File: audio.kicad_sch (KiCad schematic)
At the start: 29 parts

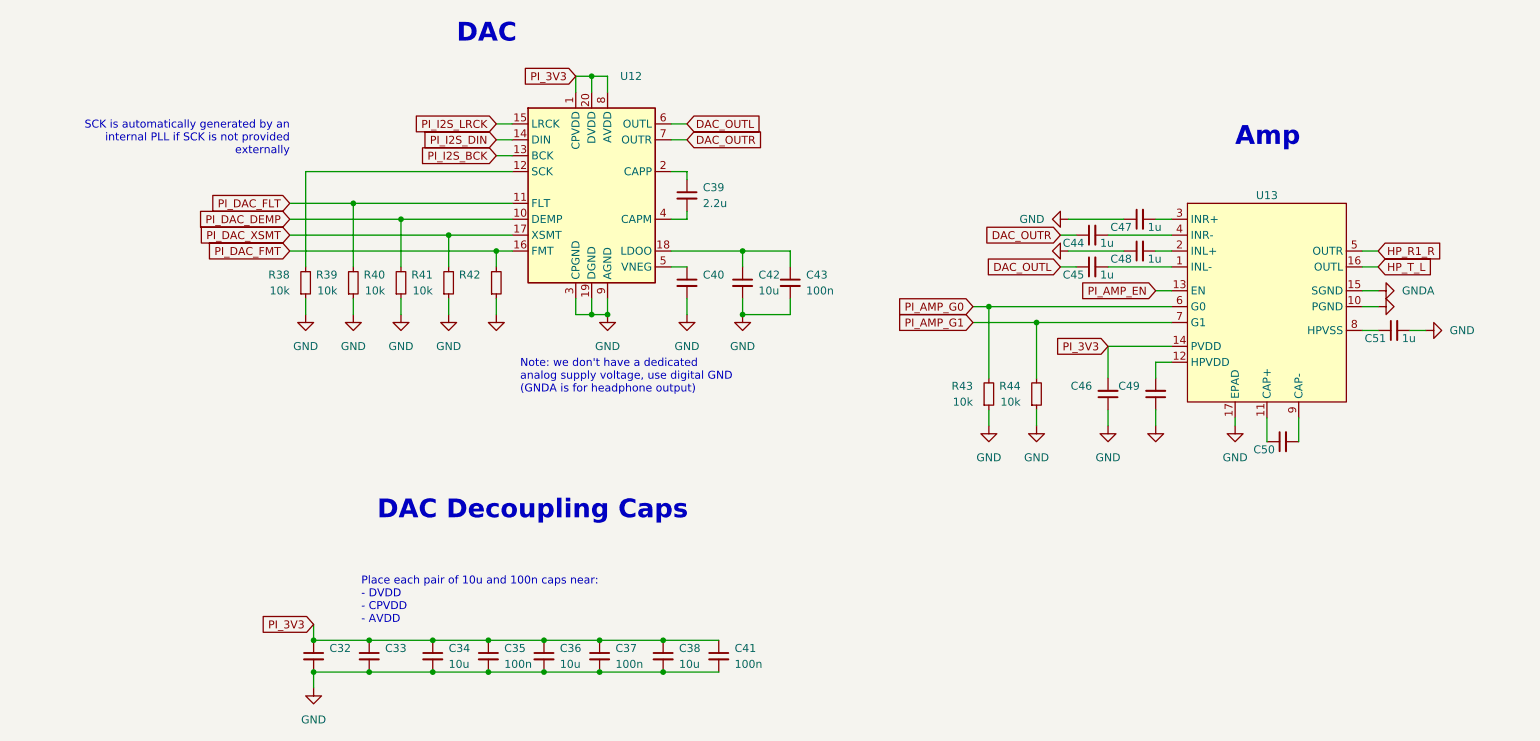
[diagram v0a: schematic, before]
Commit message: analysis: specify pi will be powered directly from VCC
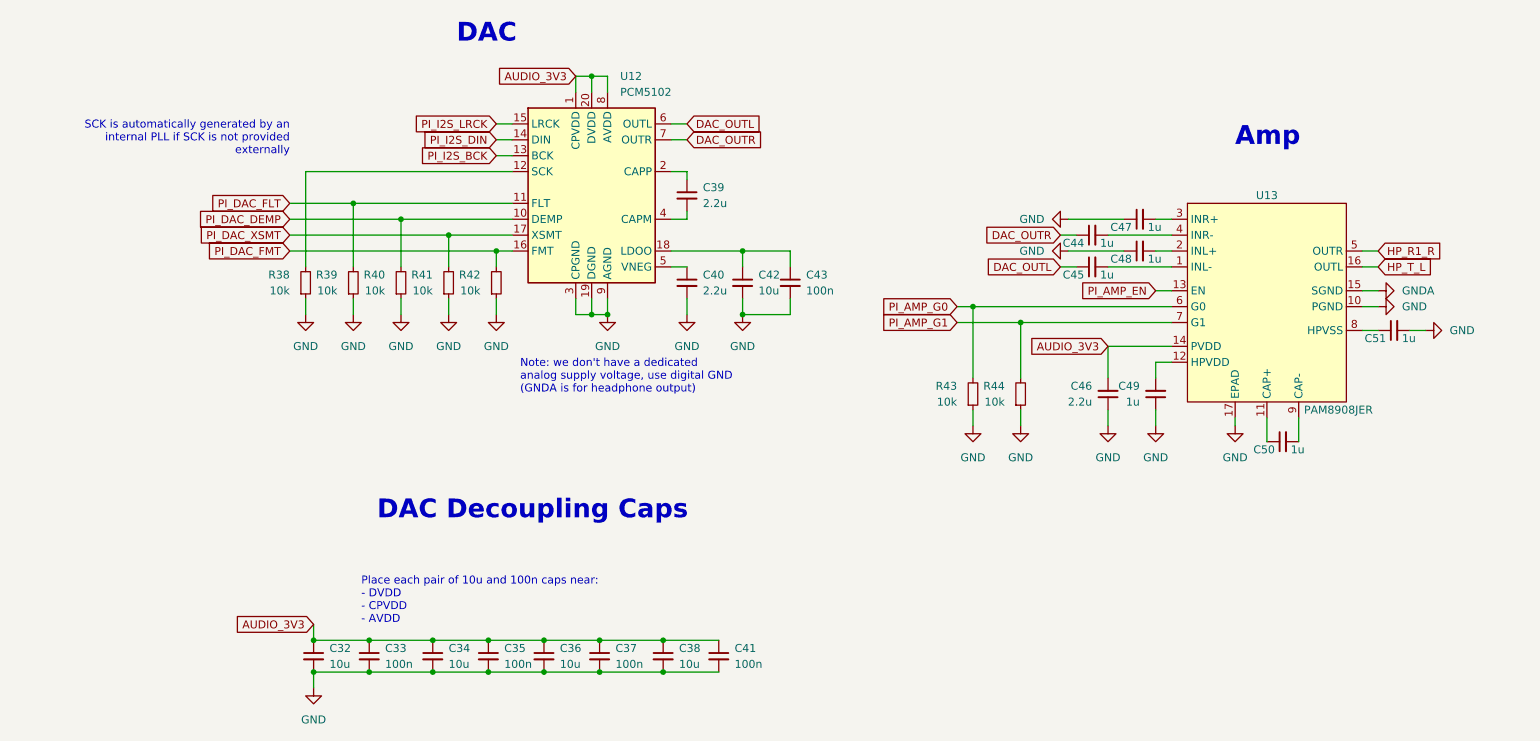
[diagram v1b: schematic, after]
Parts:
- C32: value (none) -> 10u; footprint (none) -> Capacitor_SMD:C_0402_1005Metric
- C33: value (none) -> 100n; footprint (none) -> Capacitor_SMD:C_0402_1005Metric
- C34, C35, C36, C37, C38, C39, C41, C42, C43, C44, C45, C47, C48, C51: footprint (none) -> Capacitor_SMD:C_0402_1005Metric
- C40, C46: value (none) -> 2.2u; footprint (none) -> Capacitor_SMD:C_0402_1005Metric
- C49, C50: value (none) -> 1u; footprint (none) -> Capacitor_SMD:C_0402_1005Metric
- R38, R39, R40, R41, R43, R44: footprint (none) -> Resistor_SMD:R_0402_1005Metric
- R42: value (none) -> 10k; footprint (none) -> Resistor_SMD:R_0402_1005Metric
- U12: value (none) -> PCM5102
- U13: value (none) -> PAM8908JER
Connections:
- net PI_3V3 renamed AUDIO_3V3
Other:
- moved on the sheet: R43, R44

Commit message: schem: migrate away from LCSC exclusive parts
- layout: migrate away from lcsc footprints
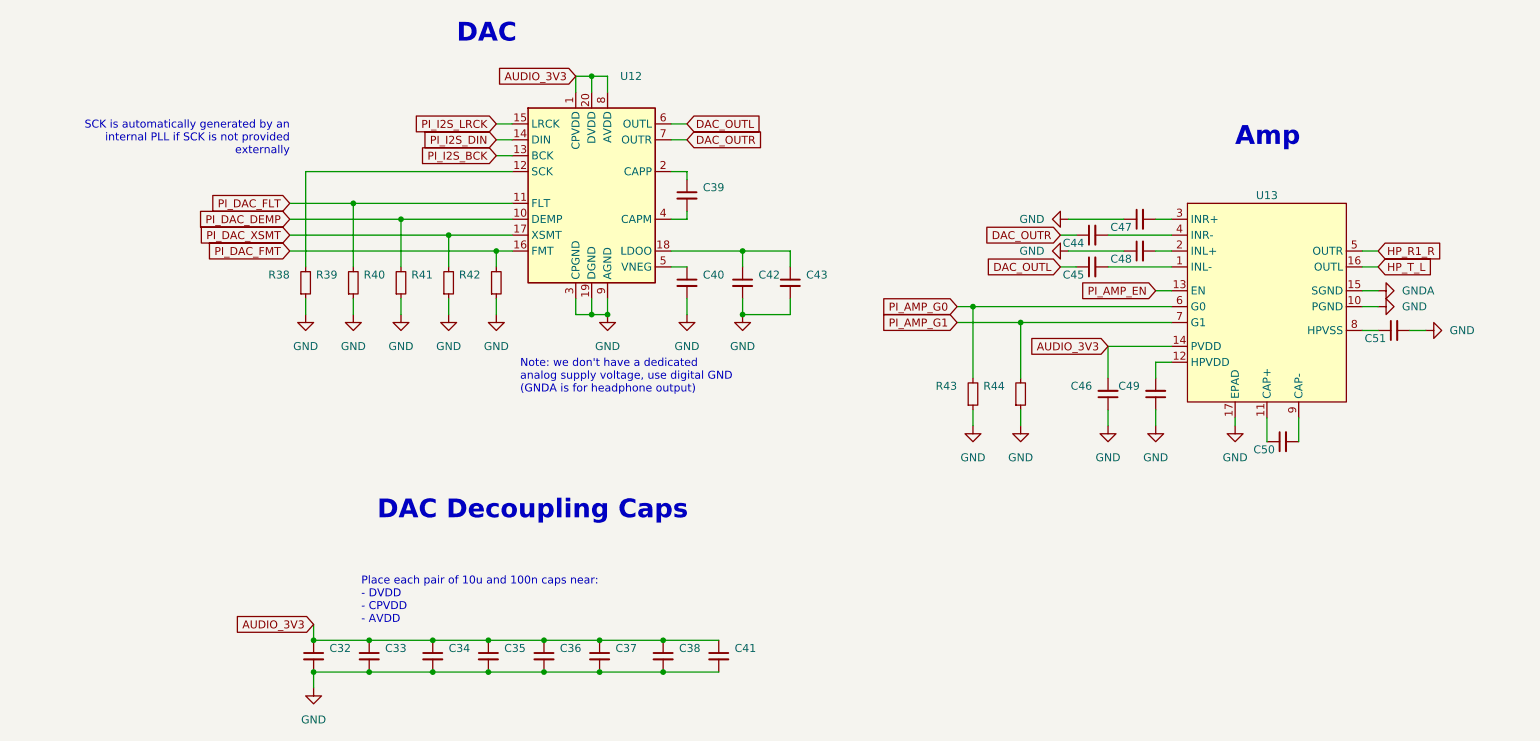
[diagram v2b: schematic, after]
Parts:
- C32, C34, C36, C38, C42: value 10u -> (none); footprint Capacitor_SMD:C_0402_1005Metric -> (none)
- C33, C35, C37, C41, C43: value 100n -> (none); footprint Capacitor_SMD:C_0402_1005Metric -> (none)
- C39, C40, C46: value 2.2u -> (none); footprint Capacitor_SMD:C_0402_1005Metric -> (none)
- C44, C45, C47, C48, C49, C50, C51: value 1u -> (none); footprint Capacitor_SMD:C_0402_1005Metric -> (none)
- R38, R39, R40, R41, R42, R43, R44: value 10k -> (none); footprint Resistor_SMD:R_0402_1005Metric -> (none)
- U12: value PCM5102 -> (none); footprint Package_SO:TSSOP-20_4.4x6.5mm_P0.65mm -> (none); Digikey Part (none) -> 296-36707-2-ND; Digikey Price/Stock (none) -> https://www.digikey.ca/en/products/detail/texas-instruments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; JLC Part (none) -> Extended Part; LCSC Part (none) -> C107671; Manufacturer (none) -> Texas Instruments; Manufacturer Part (none) -> PCM5102APWR; Mouser Part (none) -> 595-PCM5102APWR; Mouser Price/Stock (none) -> https://www.mouser.ca/ProductDetail/Texas-Instruments/PCM51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
- U13: value PAM8908JER -> (none); footprint lcsc:QFN-16_L3.0-W3.0-P0.50-BL-EP1.7 -> (none); Digikey Part (none) -> PAM8908JERDITR-ND; Digikey Price/Stock (none) -> https://www.digikey.com/en/products/detail/diodes-incorpora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; Manufacturer Part (none) -> PAM8908JER; Mouser Part (none) -> 621-PAM8908JER; Mouser Price/Stock (none) -> https://www.mouser.ca/ProductDetail/Diodes-Incorporated/PAM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

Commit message: layout: update footprint for TP4056M
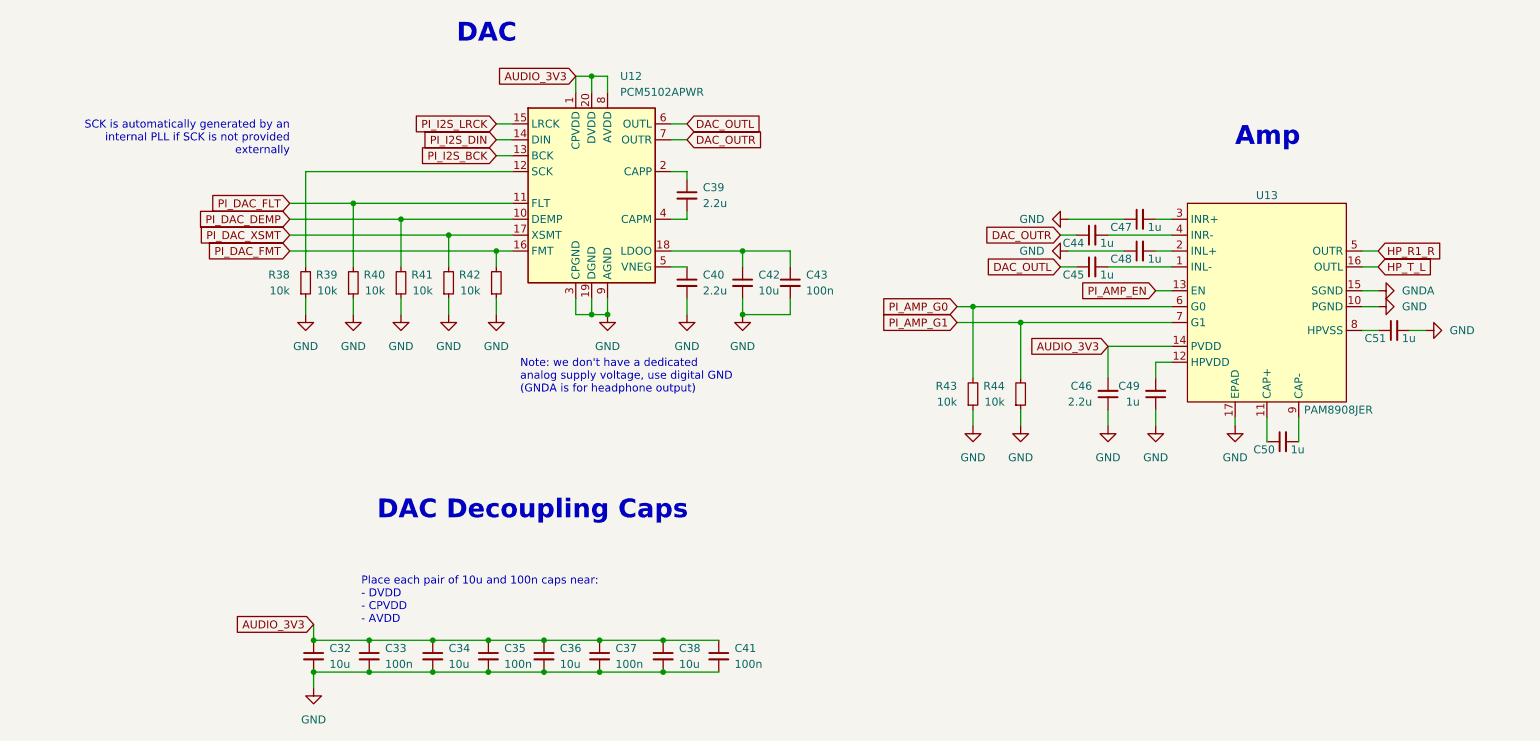
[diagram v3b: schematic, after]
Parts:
- C32, C34, C36, C38, C42: value (none) -> 10u; footprint (none) -> Capacitor_SMD:C_0402_1005Metric
- C33, C35, C37, C41, C43: value (none) -> 100n; footprint (none) -> Capacitor_SMD:C_0402_1005Metric
- C39, C40, C46: value (none) -> 2.2u; footprint (none) -> Capacitor_SMD:C_0402_1005Metric
- C44, C45, C47, C48, C49, C50, C51: value (none) -> 1u; footprint (none) -> Capacitor_SMD:C_0402_1005Metric
- R38, R39, R40, R41, R42, R43, R44: value (none) -> 10k; footprint (none) -> Resistor_SMD:R_0402_1005Metric
- U12: value (none) -> PCM5102APWR; footprint (none) -> Package_SO:TSSOP-20_4.4x6.5mm_P0.65mm
- U13: value (none) -> PAM8908JER; footprint (none) -> Package_DFN_QFN:QFN-16-1EP_3x3mm_P0.5mm_EP1.7x1.7mm

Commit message: layout: preliminary layout of most of board
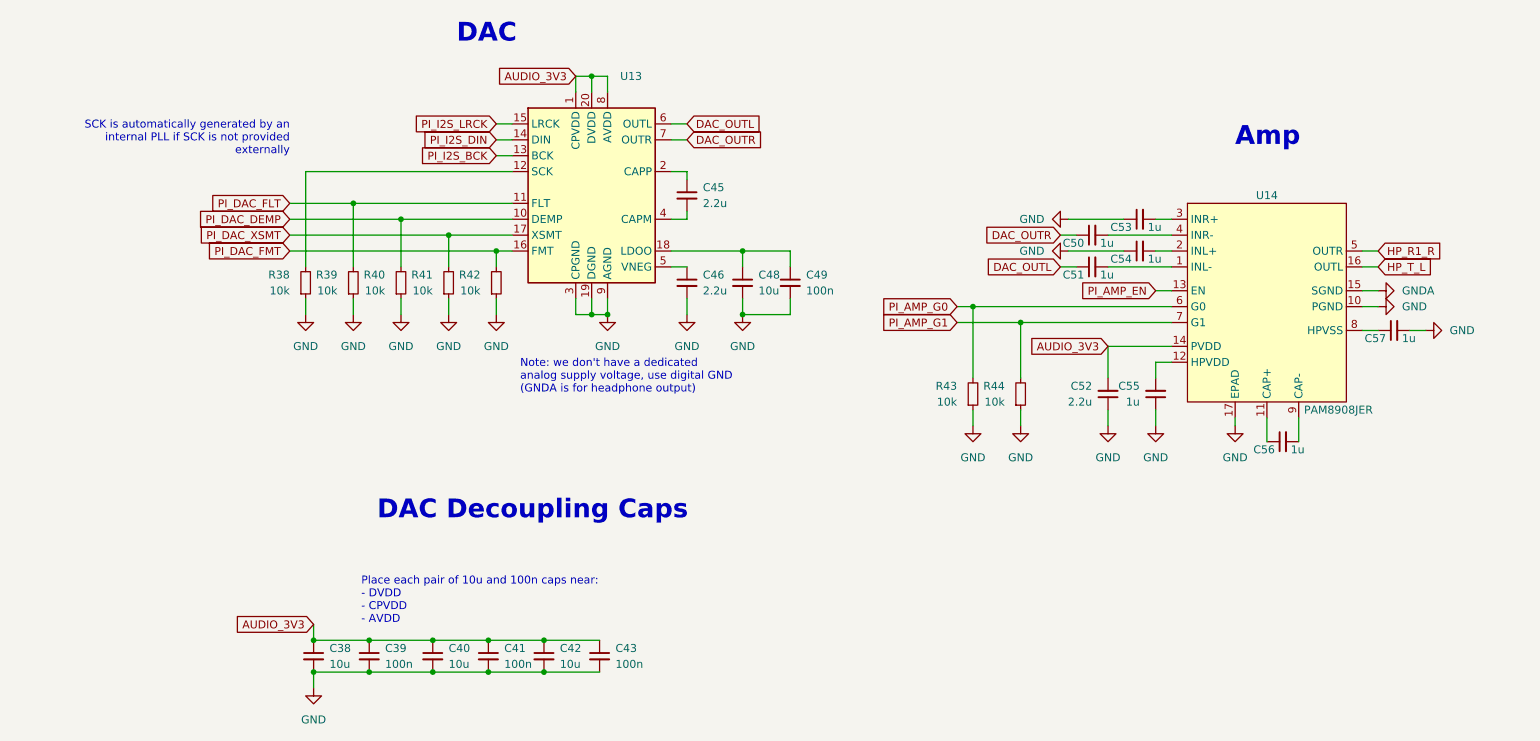
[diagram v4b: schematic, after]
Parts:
- removed C38: 10u, Capacitor_SMD:C_0402_1005Metric, symbol Device:C_Small
- removed C41: 100n, Capacitor_SMD:C_0402_1005Metric, symbol Device:C_Small
- U13: renamed from U12; value PCM5102APWR -> (none); footprint Package_SO:TSSOP-20_4.4x6.5mm_P0.65mm -> (none)
- renumbered C32 to C38, C33 to C39, C34 to C40, C35 to C41, C36 to C42, C37 to C43, C39 to C45, C40 to C46, C42 to C48, C43 to C49, C44 to C50, C45 to C51, C46 to C52, C47 to C53, C48 to C54, C49 to C55, C50 to C56, C51 to C57, U13 to U14

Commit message: routing: begin routing
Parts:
- U13: value (none) -> PCM5102APWR; footprint (none) -> Package_SO:TSSOP-20_4.4x6.5mm_P0.65mm
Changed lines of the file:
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@@
       (effects (font (size 1.27 1.27)) (justify left))
     )
-    (property "Value" "" (id 1) (at 118.8594 38.1 0)
+    (property "Value" "PCM5102APWR" (id 1) (at 118.8594 38.1 0)
       (effects (font (size 1.27 1.27)) (justify left))
     )
-    (property "Footprint" "" (id 2) (at 113.03 34.29 0)
+    (property "Footprint" "Package_SO:TSSOP-20_4.4x6.5mm_P0.65mm" (id 2) (at 113.03 34.29 0)
       (effects (font (size 1.27 1.27)) hide)
     )

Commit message: layout, routing: relayout and reroute board
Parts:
- C38, C40, C42, C48: value 10u -> (none); footprint Capacitor_SMD:C_0402_1005Metric -> (none)
- C39, C41, C43, C49: value 100n -> (none); footprint Capacitor_SMD:C_0402_1005Metric -> (none)
- C45, C46, C52: value 2.2u -> (none); footprint Capacitor_SMD:C_0402_1005Metric -> (none)
- C50, C51, C53, C54, C55, C56, C57: value 1u -> (none); footprint Capacitor_SMD:C_0402_1005Metric -> (none)
- R38, R39, R40, R41, R42, R43, R44: value 10k -> (none); footprint Resistor_SMD:R_0402_1005Metric -> (none)
- U13: value PCM5102APWR -> (none); footprint Package_SO:TSSOP-20_4.4x6.5mm_P0.65mm -> (none)
- U14: value PAM8908JER -> (none); footprint Package_DFN_QFN:QFN-16-1EP_3x3mm_P0.5mm_EP1.7x1.7mm -> (none)
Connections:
- net DAC_SCK: now reaches R38.2, U13.12 (SCK)
- net DAC_LDOO: now reaches C48.1, C49.1, U13.18 (LDOO)
- net DAC_CAPP: now reaches C45.1, U13.2 (CAPP)
- net DAC_CAPM: now reaches C45.2, U13.4 (CAPM)
- net DAC_VNEG: now reaches C46.1, U13.5 (VNEG)
- net AMP_CAP+: now reaches C56.1, U14.11 (CAP+)
- net AMP_CAP-: now reaches C56.2, U14.9 (CAP-)
- net AMP_INL-: now reaches C51.2, U14.1 (INL-)
- net AMP_HPVDD: now reaches C55.2, U14.12 (HPVDD)
- net AMP_INL+: now reaches C54.2, U14.2 (INL+)
- net AMP_INR+: now reaches C53.2, U14.3 (INR+)
- net AMP_INR-: now reaches C50.2, U14.4 (INR-)
- net AMP_HPVSS: now reaches C57.1, U14.8 (HPVSS)
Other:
- moved on the sheet: C50, C51, C52, C53, C54, C57, R43, R44

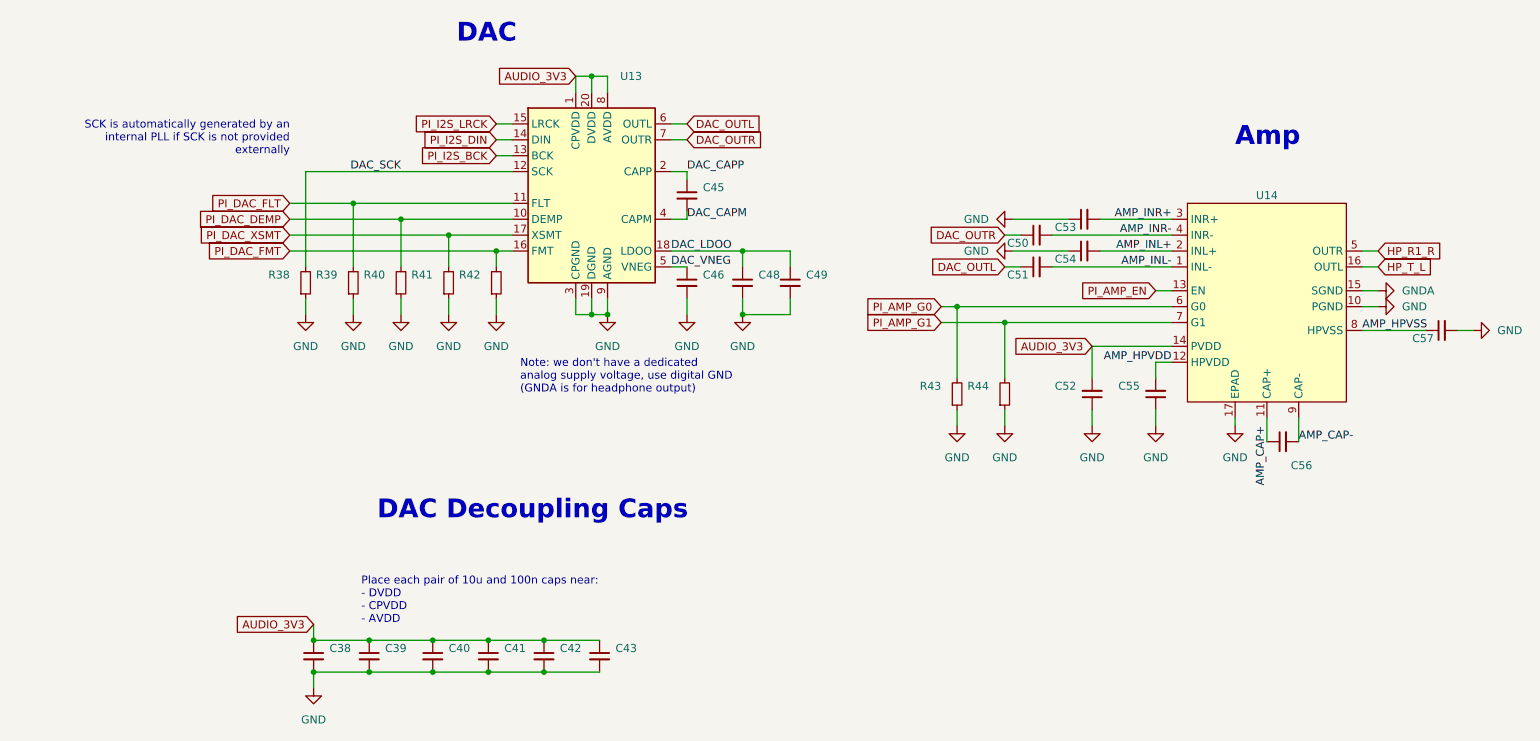
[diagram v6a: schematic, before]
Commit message: layout: add testpoints, extra mounting hole, grounding clips
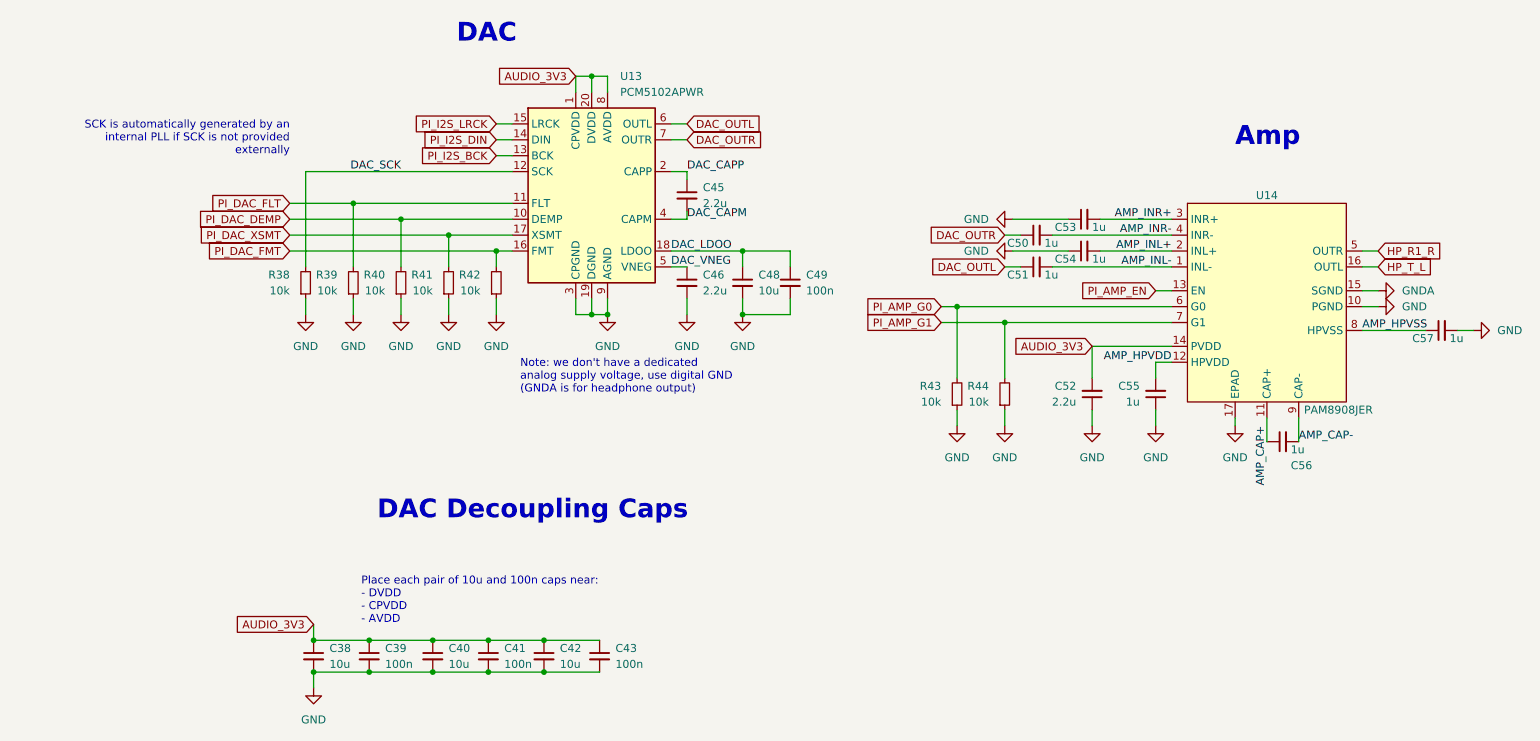
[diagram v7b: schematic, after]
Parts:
- C38, C40, C42, C48: value (none) -> 10u; footprint (none) -> Capacitor_SMD:C_0402_1005Metric
- C39, C41, C43, C49: value (none) -> 100n; footprint (none) -> Capacitor_SMD:C_0402_1005Metric
- C45, C46, C52: value (none) -> 2.2u; footprint (none) -> Capacitor_SMD:C_0402_1005Metric
- C50, C51, C53, C54, C55, C56, C57: value (none) -> 1u; footprint (none) -> Capacitor_SMD:C_0402_1005Metric
- R38, R39, R40, R41, R42, R43, R44: value (none) -> 10k; footprint (none) -> Resistor_SMD:R_0402_1005Metric
- U13: value (none) -> PCM5102APWR; footprint (none) -> Package_SO:TSSOP-20_4.4x6.5mm_P0.65mm
- U14: value (none) -> PAM8908JER; footprint (none) -> Package_DFN_QFN:QFN-16-1EP_3x3mm_P0.5mm_EP1.7x1.7mm
